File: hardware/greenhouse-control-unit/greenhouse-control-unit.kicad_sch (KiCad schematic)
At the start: 52 parts, among them J1 Buck_Conn_01x01_Female, J10 Conn_01x08, J11 Conn_01x08, J12 Conn_01x05_Female, J13 Molex_KK-396_01x08, J14 Molex_KK-254_01x05, J15 Conn_01x05_Female, J16 Conn_01x05_Female, J17 Molex_KK-254_01x04, J2 Buck_Conn_01x01_Female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

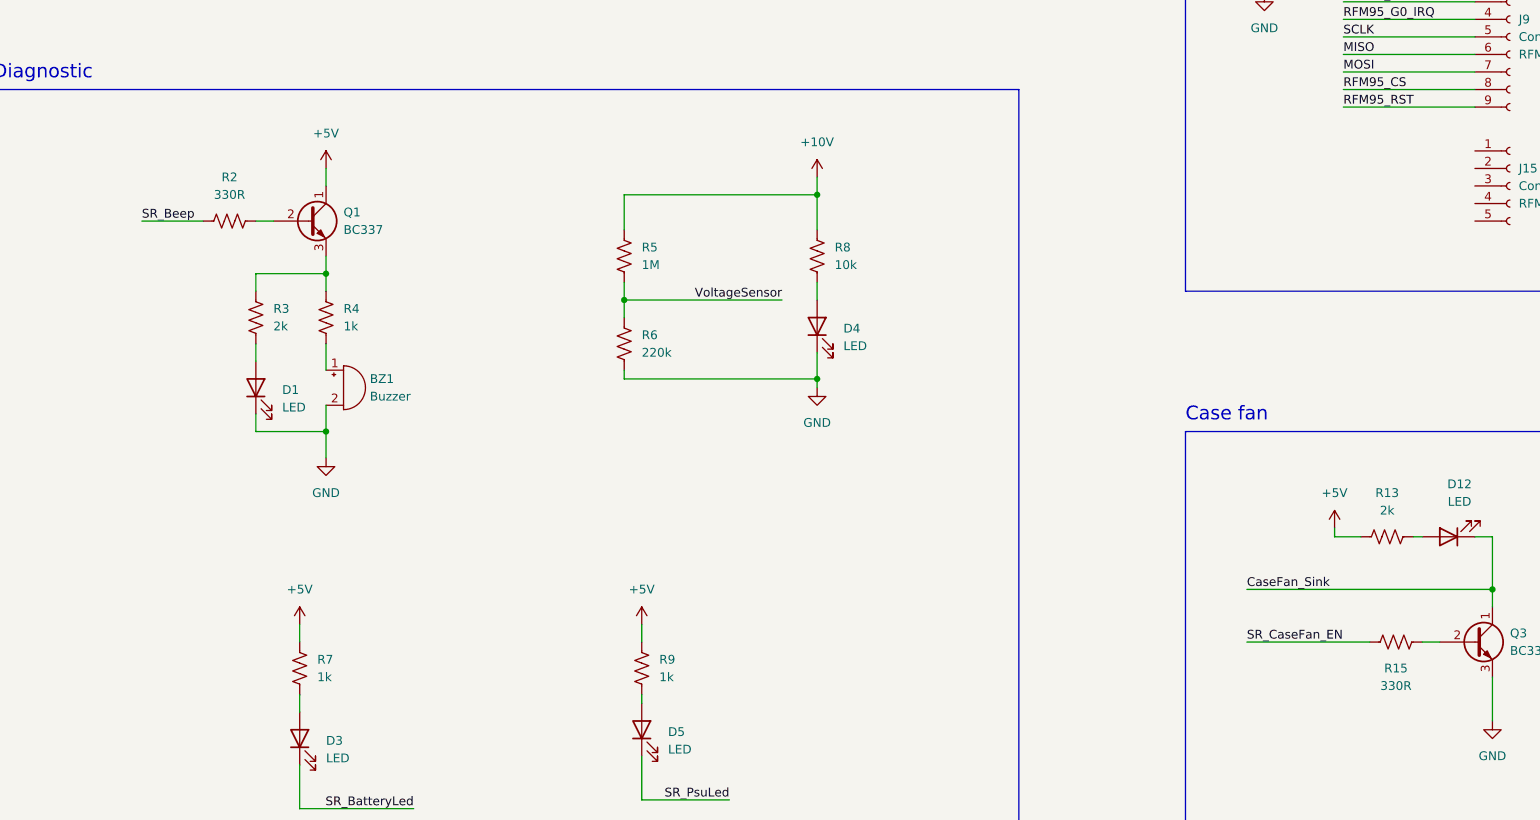
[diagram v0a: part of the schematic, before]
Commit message: Change beep BJT to sink
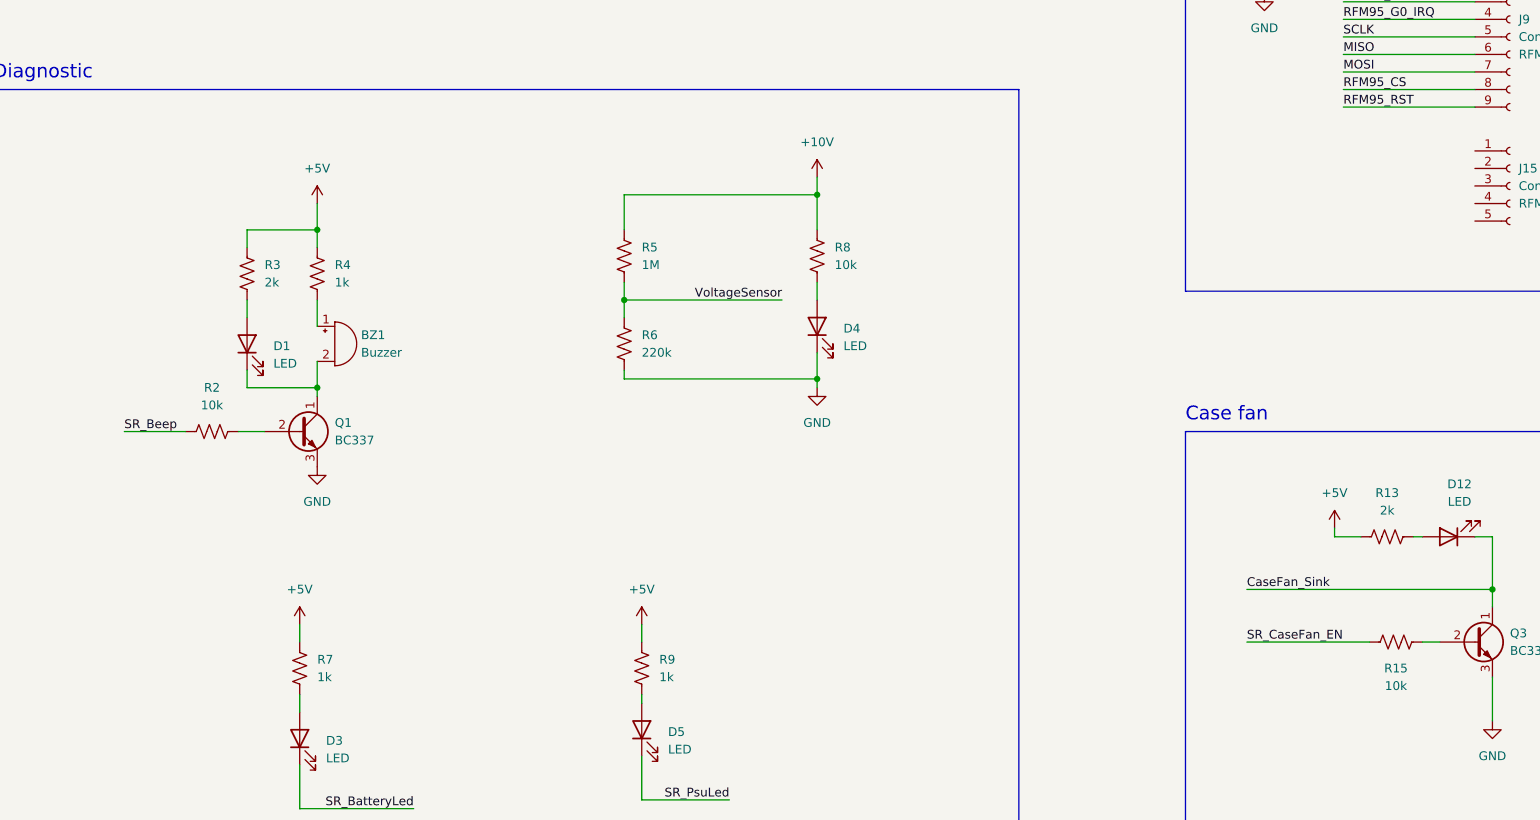
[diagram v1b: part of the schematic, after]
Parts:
- R15, R2: value 330R -> 10k
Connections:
- net +5V: now also R3.1, R4.1; no longer Q1.1 (C)
- net GND: now also Q1.3 (E); no longer BZ1.2 (+), D1.1 (K)
- new net: BZ1.2 (+), D1.1 (K), Q1.1 (C)
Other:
- moved on the sheet: BZ1, D1, Q1, R2, R3, R4

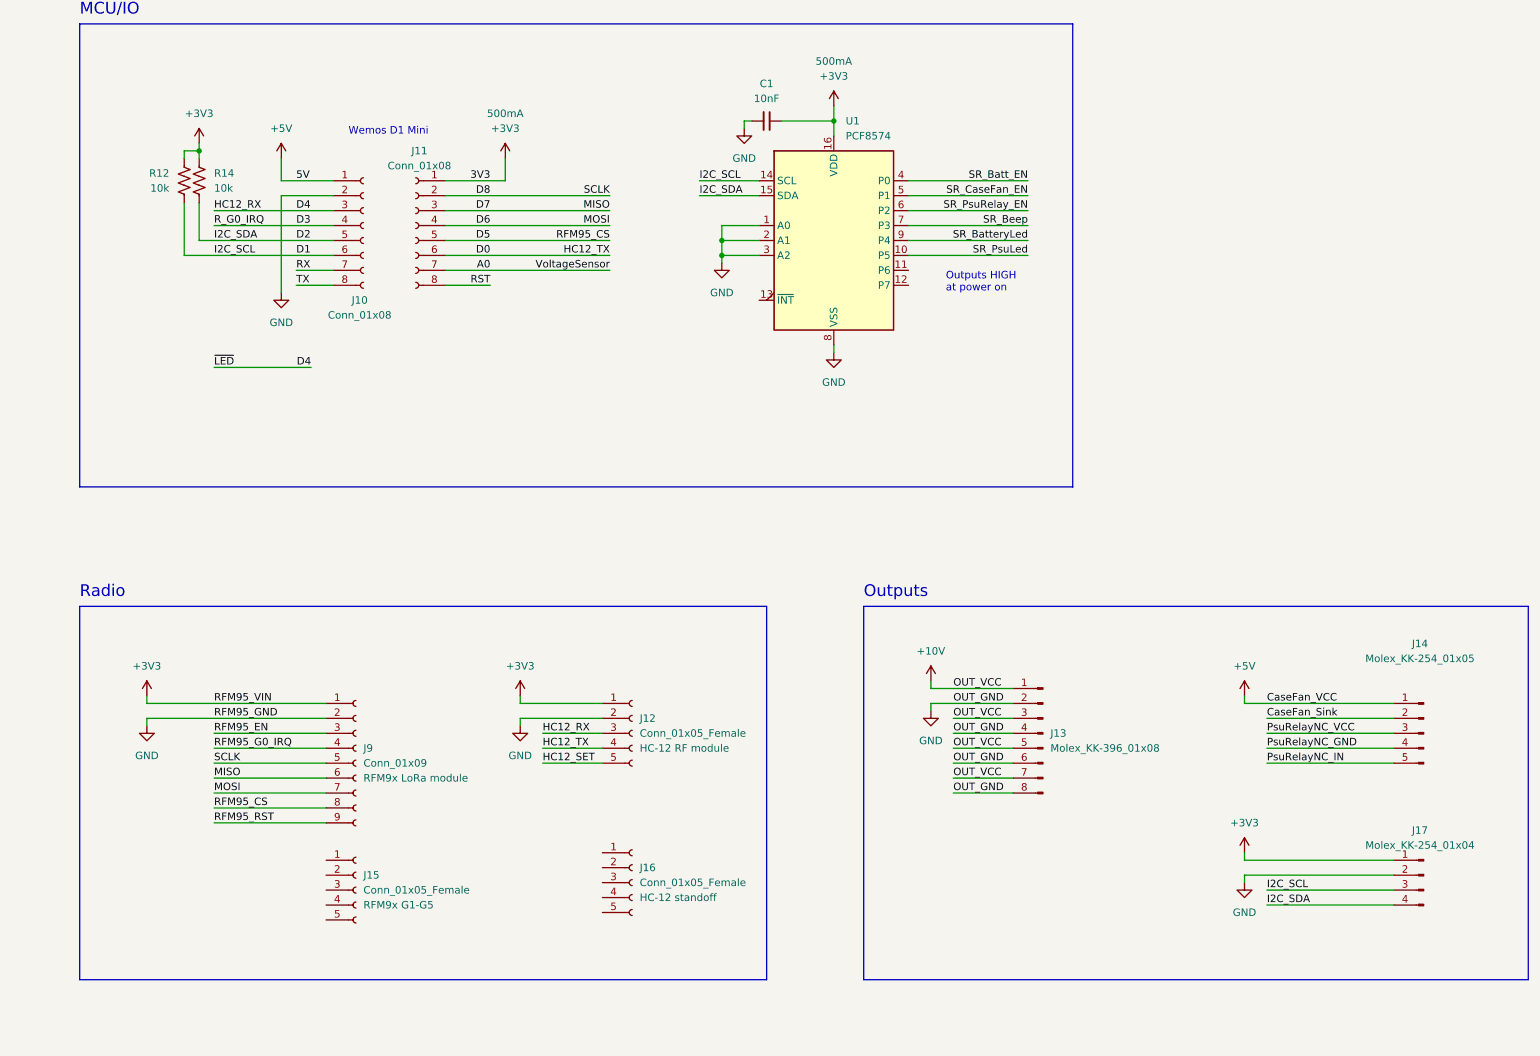
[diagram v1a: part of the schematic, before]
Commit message: Reorganised resistors
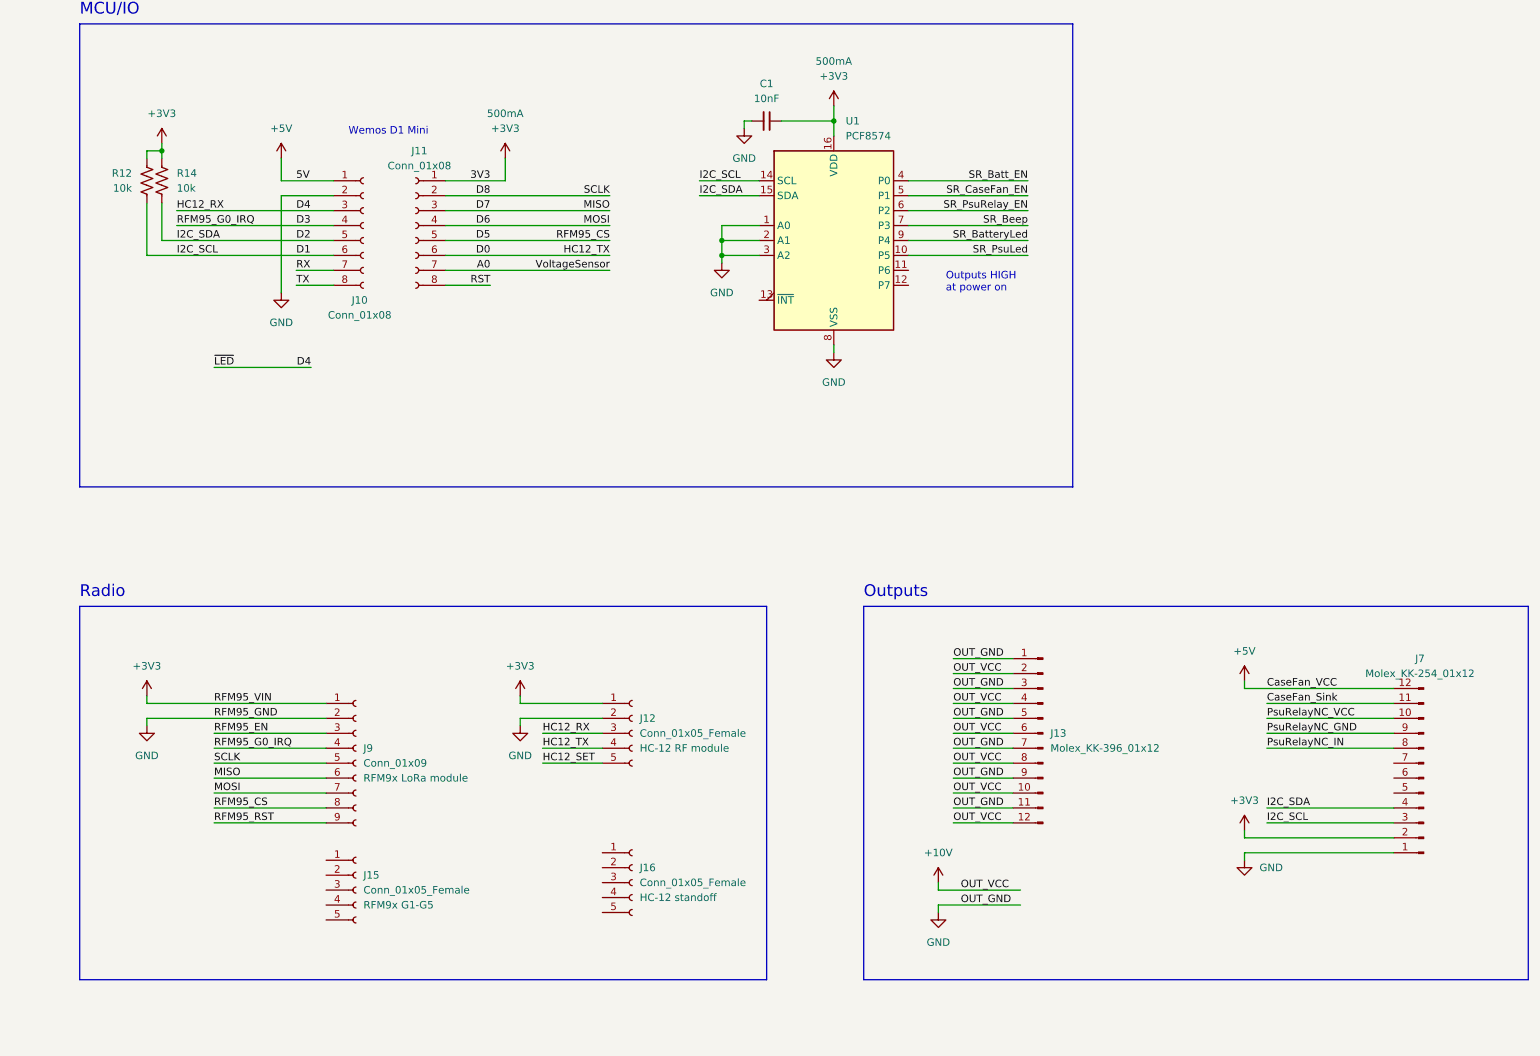
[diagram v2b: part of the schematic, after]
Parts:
- removed J14: Molex_KK-254_01x05, Connector_Molex:Molex_KK-254_AE-6410-05A_1x05_P2.54mm_Vertical, symbol Connector:Conn_01x05_Male
- removed J17: Molex_KK-254_01x04, Connector_Molex:Molex_KK-254_AE-6410-04A_1x04_P2.54mm_Vertical, symbol Connector:Conn_01x04_Male
- added J7: Molex_KK-254_01x12, Connector_Molex:Molex_KK-254_AE-6410-12A_1x12_P2.54mm_Vertical, symbol Connector:Conn_01x12_Male
- J13: value Molex_KK-396_01x08 -> Molex_KK-396_01x12; footprint Connector_Molex:Molex_KK-396_A-41791-0008_1x08_P3.96mm_Vertical -> Connector_Molex:Molex_KK-396_A-41791-0012_1x12_P3.96mm_Vertical; symbol Connector:Conn_01x08_Male -> Connector:Conn_01x12_Male
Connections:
- net RFM95_G0_IRQ is gone; now on net D3: J9.4 (Pin_4)
- net +10V: now also J13.10 (Pin_10), J13.12 (Pin_12), J13.2 (Pin_2), J13.4 (Pin_4), J13.6 (Pin_6), J13.8 (Pin_8), J7.10 (Pin_10); no longer J13.1 (Pin_1), J13.3 (Pin_3), J13.5 (Pin_5), J13.7 (Pin_7)
- net +3V3: now also J7.2 (Pin_2)
- net +5V: now also J7.12 (Pin_12)
- net CaseFan_Sink: now also J7.11 (Pin_11)
- net D1: now also J7.3 (Pin_3)
- net D2: now also J7.4 (Pin_4)
- net GND: now also J13.1 (Pin_1), J13.11 (Pin_11), J13.3 (Pin_3), J13.5 (Pin_5), J13.7 (Pin_7), J13.9 (Pin_9), J7.1 (Pin_1), J7.9 (Pin_9); no longer J13.2 (Pin_2), J13.4 (Pin_4), J13.6 (Pin_6), J13.8 (Pin_8)
- net PsuRelayNC_IN: now also J7.8 (Pin_8)
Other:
- moved on the sheet: R12, R14

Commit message: Reverse connectors
Now correct way
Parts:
- removed J13: Molex_KK-396_01x12, Connector_Molex:Molex_KK-396_A-41791-0012_1x12_P3.96mm_Vertical, symbol Connector:Conn_01x12_Male
- removed J5, J6: Molex_KK-396_01x02, Connector_Molex:Molex_KK-396_A-41791-0002_1x02_P3.96mm_Vertical, symbol Connector:Conn_01x02_Male
- removed J7: Molex_KK-254_01x12, Connector_Molex:Molex_KK-254_AE-6410-12A_1x12_P2.54mm_Vertical, symbol Connector:Conn_01x12_Male
- added J?: Molex_KK-396_01x12, Connector_Molex:Molex_KK-396_A-41791-0012_1x12_P3.96mm_Vertical, symbol Connector:Conn_01x12_Male
- added J? (x2): Molex_KK-396_01x02, Connector_Molex:Molex_KK-396_A-41791-0002_1x02_P3.96mm_Vertical, symbol Connector:Conn_01x02_Male
- added J?: Molex_KK-254_01x12, Connector_Molex:Molex_KK-254_AE-6410-12A_1x12_P2.54mm_Vertical, symbol Connector:Conn_01x12_Male
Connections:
- net +10V: now also J?.1 (Pin_1), J?.1 (Pin_1), J?.1 (Pin_1), J?.11 (Pin_11), J?.3 (Pin_3), J?.3 (Pin_3), J?.5 (Pin_5), J?.7 (Pin_7), J?.9 (Pin_9)
- net +3V3: now also J?.11 (Pin_11)
- net +5V: now also J?.1 (Pin_1)
- net Batt_GND: now also J?.2 (Pin_2)
- net CaseFan_Sink: now also J?.2 (Pin_2)
- net D1: now also J?.10 (Pin_10)
- net D2: now also J?.9 (Pin_9)
- net GND: now also J?.10 (Pin_10), J?.12 (Pin_12), J?.12 (Pin_12), J?.2 (Pin_2), J?.2 (Pin_2), J?.4 (Pin_4), J?.4 (Pin_4), J?.6 (Pin_6), J?.8 (Pin_8)
- net PsuRelayNC_IN: now also J?.5 (Pin_5)

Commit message: Tidy up plane islands
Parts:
- R7, R9: value 1k -> 2k
- gave numbers to parts that had none: 4
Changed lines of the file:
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@@
   (symbol (lib_id "Connector:Conn_01x12_Male") (at 453.39 172.72 0) (mirror y) (unit 1)
     (in_bom yes) (on_board yes) (fields_autoplaced)
-    (property "Reference" "J?" (id 0) (at 454.66 172.7199 0)
+    (property "Reference" "J7" (id 0) (at 454.66 172.7199 0)
       (effects (font (size 1.27 1.27)) (justify right))
     )
@@
   (symbol (lib_id "Connector:Conn_01x02_Male") (at 162.56 64.77 0) (unit 1)
     (in_bom yes) (on_board yes) (fields_autoplaced)
-    (property "Reference" "J?" (id 0) (at 161.29 64.7699 0)
+    (property "Reference" "J6" (id 0) (at 161.29 64.7699 0)
       (effects (font (size 1.27 1.27)) (justify right))
     )
@@
   (symbol (lib_id "Connector:Conn_01x12_Male") (at 521.97 177.8 0) (mirror y) (unit 1)
     (in_bom yes) (on_board yes) (fields_autoplaced)
-    (property "Reference" "J?" (id 0) (at 521.335 160.02 0))
+    (property "Reference" "J8" (id 0) (at 521.335 160.02 0))
     (property "Value" "Molex_KK-254_01x12" (id 1) (at 521.335 162.56 0))
     (property "Footprint" "Connector_Molex:Molex_KK-254_AE-6410-12A_1x12_P2.54mm_Vertical" (id 2) (at 521.97 177.8 0)
@@
       (effects (font (size 1.27 1.27)) (justify left))
     )
-    (property "Value" "1k" (id 1) (at 217.17 270.5099 0)
+    (property "Value" "2k" (id 1) (at 217.17 270.5099 0)
       (effects (font (size 1.27 1.27)) (justify left))
     )
@@
       (effects (font (size 1.27 1.27)) (justify left))
     )
-    (property "Value" "1k" (id 1) (at 167.64 270.5099 0)
+    (property "Value" "2k" (id 1) (at 167.64 270.5099 0)
       (effects (font (size 1.27 1.27)) (justify left))
     )
@@
   (symbol (lib_id "Connector:Conn_01x02_Male") (at 161.29 78.74 0) (unit 1)
     (in_bom yes) (on_board yes) (fields_autoplaced)
-    (property "Reference" "J?" (id 0) (at 160.02 78.7399 0)
+    (property "Reference" "J5" (id 0) (at 160.02 78.7399 0)
       (effects (font (size 1.27 1.27)) (justify right))
     )
@@
       (reference "J4") (unit 1) (value "Buck_Conn_01x01_Female") (footprint "Connector_Pin:Pin_D1.0mm_L10.0mm")
     )
+    (path "/c551cebd-0bd3-47ba-856a-e27d4df314b5"
+      (reference "J5") (unit 1) (value "Molex_KK-396_01x02") (footprint "Connector_Molex:Molex_KK-396_A-41791-0002_1x02_P3.96mm_Vertical")
+    )
+    (path "/5357994b-4f7f-427c-9ac3-7bcbcc4a8a94"
+      (reference "J6") (unit 1) (value "Molex_KK-396_01x02") (footprint "Connector_Molex:Molex_KK-396_A-41791-0002_1x02_P3.96mm_Vertical")
+    )
+    (path "/47527e0b-7bb0-4b6f-a4d0-d033c29db61d"
+      (reference "J7") (unit 1) (value "Molex_KK-396_01x12") (footprint "Connector_Molex:Molex_KK-396_A-41791-0012_1x12_P3.96mm_Vertical")
+    )
+    (path "/ab8c1269-ccb7-406f-a043-b4d752d2d67f"
+      (reference "J8") (unit 1) (value "Molex_KK-254_01x12") (footprint "Connector_Molex:Molex_KK-254_AE-6410-12A_1x12_P2.54mm_Vertical")
+    )
     (path "/b9363158-cf9b-401f-be76-ff2c499c3f4a"
       (reference "J9") (unit 1) (value "Conn_01x09") (footprint "Connector_PinSocket_2.54mm:PinSocket_1x09_P2.54mm_Vertical")
@@
       (reference "J16") (unit 1) (value "Conn_01x05_Female") (footprint "Connector_PinSocket_2.54mm:PinSocket_1x05_P2.54mm_Vertical")
     )
-    (path "/47527e0b-7bb0-4b6f-a4d0-d033c29db61d"
-      (reference "J?") (unit 1) (value "Molex_KK-396_01x12") (footprint "Connector_Molex:Molex_KK-396_A-41791-0012_1x12_P3.96mm_Vertical")
-    )
-    (path "/5357994b-4f7f-427c-9ac3-7bcbcc4a8a94"
-      (reference "J?") (unit 1) (value "Molex_KK-396_01x02") (footprint "Connector_Molex:Molex_KK-396_A-41791-0002_1x02_P3.96mm_Vertical")
-    )
-    (path "/ab8c1269-ccb7-406f-a043-b4d752d2d67f"
-      (reference "J?") (unit 1) (value "Molex_KK-254_01x12") (footprint "Connector_Molex:Molex_KK-254_AE-6410-12A_1x12_P2.54mm_Vertical")
-    )
-    (path "/c551cebd-0bd3-47ba-856a-e27d4df314b5"
-      (reference "J?") (unit 1) (value "Molex_KK-396_01x02") (footprint "Connector_Molex:Molex_KK-396_A-41791-0002_1x02_P3.96mm_Vertical")
-    )
     (path "/56c51bb9-1b0c-4751-b4b4-bb794b284a48"
       (reference "Q1") (unit 1) (value "BC337") (footprint "Package_TO_SOT_THT:TO-92_Inline")
@@
     )
     (path "/bf3469a0-b31c-4b25-9d5b-5d728857d06e"
-      (reference "R7") (unit 1) (value "1k") (footprint "Resistor_THT:R_Axial_DIN0207_L6.3mm_D2.5mm_P7.62mm_Horizontal")
+      (reference "R7") (unit 1) (value "2k") (footprint "Resistor_THT:R_Axial_DIN0207_L6.3mm_D2.5mm_P7.62mm_Horizontal")
     )
     (path "/b009fdd3-7e21-47db-96d1-b943d0c29b40"
@@
     )
     (path "/b238b697-aa1a-48c1-94dc-f87c7c856aeb"
-      (reference "R9") (unit 1) (value "1k") (footprint "Resistor_THT:R_Axial_DIN0207_L6.3mm_D2.5mm_P7.62mm_Horizontal")
+      (reference "R9") (unit 1) (value "2k") (footprint "Resistor_THT:R_Axial_DIN0207_L6.3mm_D2.5mm_P7.62mm_Horizontal")
     )
     (path "/70734713-5079-4de4-862c-a002f5353029"

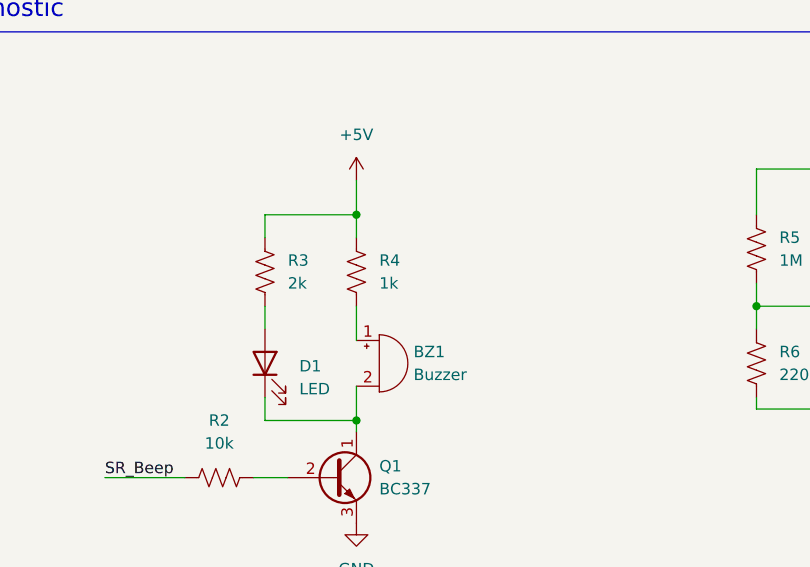
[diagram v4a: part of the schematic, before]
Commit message: Changed to 4 layer board
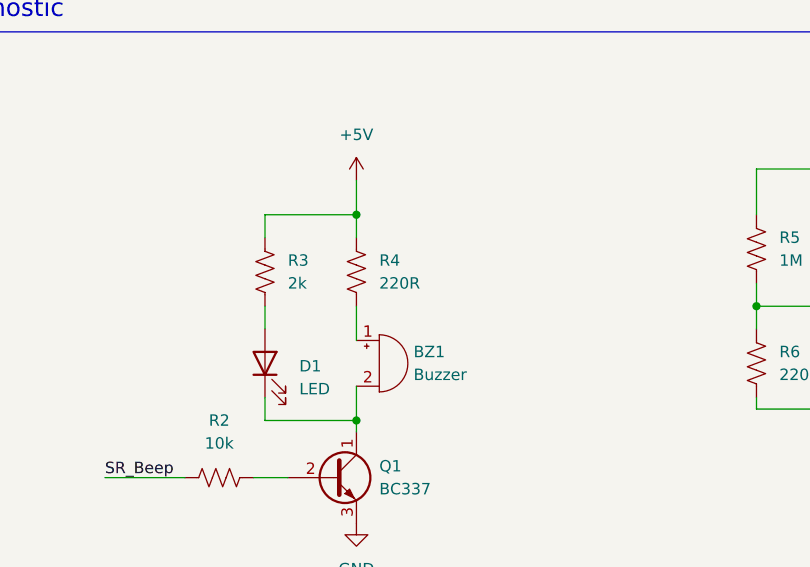
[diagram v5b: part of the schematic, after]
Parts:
- R4: value 1k -> 220R
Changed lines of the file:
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@@
       (effects (font (size 1.27 1.27)) (justify left))
     )
-    (property "Value" "1k" (id 1) (at 170.18 213.3599 0)
+    (property "Value" "220R" (id 1) (at 170.18 213.3599 0)
       (effects (font (size 1.27 1.27)) (justify left))
     )
@@
     )
     (path "/857a7d8e-c70a-4041-ab4d-018ea734a2fb"
-      (reference "R4") (unit 1) (value "1k") (footprint "Resistor_THT:R_Axial_DIN0207_L6.3mm_D2.5mm_P7.62mm_Horizontal")
+      (reference "R4") (unit 1) (value "220R") (footprint "Resistor_THT:R_Axial_DIN0207_L6.3mm_D2.5mm_P7.62mm_Horizontal")
     )
     (path "/cfa38080-e348-4bf2-a0c4-dc9062a9cc79"
